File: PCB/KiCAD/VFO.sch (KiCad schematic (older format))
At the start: 23 parts, among them CON1 AVR-ISP-6, J1 USB_OTG, U10 LD1117S33TR, U2 ATMEGA8-16AU, U3 ADuM1201CR, U6 FT232RL, U7 SI5351, Y7 8Mhz, Y8 27Mhz

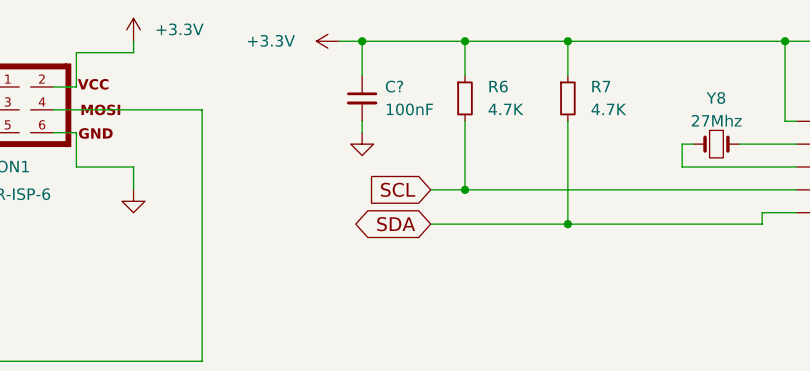
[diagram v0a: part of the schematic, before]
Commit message: diode mixer on discrete components, begin move to DragonFly libs
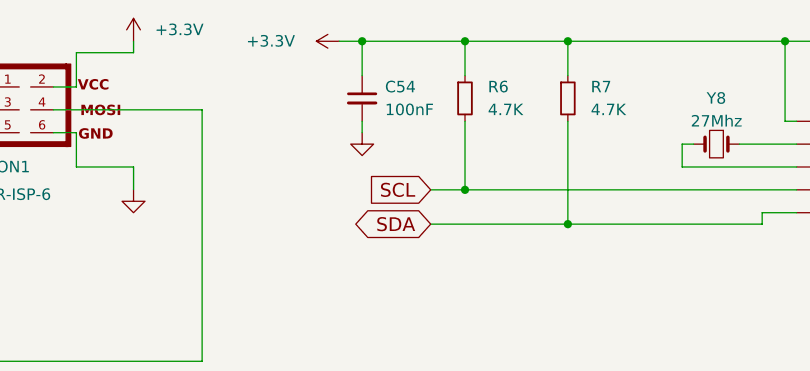
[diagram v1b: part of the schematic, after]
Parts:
- U10: footprint TO_SOT_Packages_SMD:SOT-223 -> DragonFly:SOT-223
- U3: footprint Housings_SOIC:SOIC-8_3.9x4.9mm_Pitch1.27mm -> DragonFly:SOIC-8_3.9x4.9mm_Pitch1.27mm
- gave numbers to parts that had none: 1
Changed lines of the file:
@@
 EESchema Schematic File Version 2
 LIBS:DragonFly-rescue
-LIBS:bee-rescue
 LIBS:power
 LIBS:device
@@
 $EndComp
 $Comp
-L GND #PWR39
+L GND #PWR023
 U 1 1 589EB3CB
 P 6100 1350
-F 0 "#PWR39" H 6100 1100 50  0001 C CNN
+F 0 "#PWR023" H 6100 1100 50  0001 C CNN
 F 1 "GND" H 6100 1200 50  0001 C CNN
 F 2 "" H 6100 1350 50  0000 C CNN
@@
 $EndComp
 $Comp
-L GND #PWR24
+L GND #PWR024
 U 1 1 589EFCBC
 P 750 2350
-F 0 "#PWR24" H 750 2100 50  0001 C CNN
+F 0 "#PWR024" H 750 2100 50  0001 C CNN
 F 1 "GND" H 750 2200 50  0001 C CNN
 F 2 "" H 750 2350 50  0000 C CNN
@@
 $EndComp
 $Comp
-L GND #PWR25
+L GND #PWR025
 U 1 1 589EFDB6
 P 750 2800
-F 0 "#PWR25" H 750 2550 50  0001 C CNN
+F 0 "#PWR025" H 750 2550 50  0001 C CNN
 F 1 "GND" H 750 2650 50  0001 C CNN
 F 2 "" H 750 2800 50  0000 C CNN
@@
 $EndComp
 $Comp
-L +3.3V #PWR41
+L +3.3V #PWR026
 U 1 1 58A03CC8
 P 7000 700
-F 0 "#PWR41" H 7000 550 50  0001 C CNN
+F 0 "#PWR026" H 7000 550 50  0001 C CNN
 F 1 "+3.3V" V 7000 1000 50  0000 C CNN
 F 2 "" H 7000 700 50  0000 C CNN
@@
 $EndComp
 $Comp
-L GND #PWR31
+L GND #PWR027
 U 1 1 58A061EE
 P 2850 6550
-F 0 "#PWR31" H 2850 6300 50  0001 C CNN
+F 0 "#PWR027" H 2850 6300 50  0001 C CNN
 F 1 "GND" H 2850 6400 50  0001 C CNN
 F 2 "" H 2850 6550 50  0000 C CNN
@@
 $EndComp
 $Comp
-L GND #PWR32
+L GND #PWR028
 U 1 1 58A09E30
 P 3400 6900
-F 0 "#PWR32" H 3400 6650 50  0001 C CNN
+F 0 "#PWR028" H 3400 6650 50  0001 C CNN
 F 1 "GND" H 3400 6750 50  0001 C CNN
 F 2 "" H 3400 6900 50  0000 C CNN
@@
 $EndComp
 $Comp
-L GND #PWR33
+L GND #PWR029
 U 1 1 58A0C9D9
 P 4150 6900
-F 0 "#PWR33" H 4150 6650 50  0001 C CNN
+F 0 "#PWR029" H 4150 6650 50  0001 C CNN
 F 1 "GND" H 4150 6750 50  0001 C CNN
 F 2 "" H 4150 6900 50  0000 C CNN
@@
 BFO_TX
 $Comp
-L GND #PWR48
+L GND #PWR030
 U 1 1 58E0B7EA
 P 10400 1250
-F 0 "#PWR48" H 10400 1000 50  0001 C CNN
+F 0 "#PWR030" H 10400 1000 50  0001 C CNN
 F 1 "GND" H 10400 1100 50  0001 C CNN
 F 2 "" H 10400 1250 50  0000 C CNN
@@
 SCL
 $Comp
-L +3.3V #PWR38
+L +3.3V #PWR031
 U 1 1 60FBBB98
 P 6100 700
-F 0 "#PWR38" H 6100 550 50  0001 C CNN
+F 0 "#PWR031" H 6100 550 50  0001 C CNN
 F 1 "+3.3V" H 6300 750 50  0000 C CNN
 F 2 "" H 6100 700 50  0000 C CNN
@@
 F 0 "U3" H 4750 4600 50  0000 L CNN
 F 1 "ADuM1201CR" H 5100 4600 50  0000 L CNN
-F 2 "Housings_SOIC:SOIC-8_3.9x4.9mm_Pitch1.27mm" H 5100 4200 50  0001 C CIN
+F 2 "DragonFly:SOIC-8_3.9x4.9mm_Pitch1.27mm" H 5100 4200 50  0001 C CIN
 F 3 "" H 5100 4200 50  0001 C CNN
 	1    5100 4200
@@
 $EndComp
 $Comp
-L GND #PWR35
+L GND #PWR032
 U 1 1 60FBEFE8
 P 4550 4450
-F 0 "#PWR35" H 4550 4200 50  0001 C CNN
+F 0 "#PWR032" H 4550 4200 50  0001 C CNN
 F 1 "GND" H 4550 4300 50  0001 C CNN
 F 2 "" H 4550 4450 50  0000 C CNN
@@
 $EndComp
 $Comp
-L +3.3V #PWR34
+L +3.3V #PWR033
 U 1 1 60FBF348
 P 4550 3950
-F 0 "#PWR34" H 4550 3800 50  0001 C CNN
+F 0 "#PWR033" H 4550 3800 50  0001 C CNN
 F 1 "+3.3V" V 4550 4200 50  0000 C CNN
 F 2 "" H 4550 3950 50  0000 C CNN
@@
 $EndComp
 $Comp
-L GNDD #PWR44
+L GNDD #PWR034
 U 1 1 60FC3E83
 P 8650 4700
-F 0 "#PWR44" H 8650 4450 50  0001 C CNN
+F 0 "#PWR034" H 8650 4450 50  0001 C CNN
 F 1 "GNDD" H 8650 4575 50  0001 C CNN
 F 2 "" H 8650 4700 50  0001 C CNN
@@
 $EndComp
 $Comp
-L GNDD #PWR43
+L GNDD #PWR035
 U 1 1 60FC3F82
 P 8650 4000
-F 0 "#PWR43" H 8650 3750 50  0001 C CNN
+F 0 "#PWR035" H 8650 3750 50  0001 C CNN
 F 1 "GNDD" H 8650 3875 50  0001 C CNN
 F 2 "" H 8650 4000 50  0001 C CNN
@@
 $EndComp
 $Comp
-L GNDD #PWR47
+L GNDD #PWR036
 U 1 1 60FC3FE1
 P 10250 4750
-F 0 "#PWR47" H 10250 4500 50  0001 C CNN
+F 0 "#PWR036" H 10250 4500 50  0001 C CNN
 F 1 "GNDD" H 10250 4625 50  0001 C CNN
 F 2 "" H 10250 4750 50  0001 C CNN
@@
 $EndComp
 $Comp
-L GNDD #PWR37
+L GNDD #PWR037
 U 1 1 60FC45C5
 P 5650 4450
-F 0 "#PWR37" H 5650 4200 50  0001 C CNN
+F 0 "#PWR037" H 5650 4200 50  0001 C CNN
 F 1 "GNDD" H 5650 4325 50  0001 C CNN
 F 2 "" H 5650 4450 50  0001 C CNN
@@
 $EndComp
 $Comp
-L GNDD #PWR40
+L GNDD #PWR038
 U 1 1 60FC465C
 P 7000 5900
-F 0 "#PWR40" H 7000 5650 50  0001 C CNN
+F 0 "#PWR038" H 7000 5650 50  0001 C CNN
 F 1 "GNDD" H 7000 5775 50  0001 C CNN
 F 2 "" H 7000 5900 50  0001 C CNN
@@
 $EndComp
 $Comp
-L GNDD #PWR45
+L GNDD #PWR039
 U 1 1 60FC82A8
 P 8700 3600
-F 0 "#PWR45" H 8700 3350 50  0001 C CNN
+F 0 "#PWR039" H 8700 3350 50  0001 C CNN
 F 1 "GNDD" H 8700 3475 50  0001 C CNN
 F 2 "" H 8700 3600 50  0001 C CNN
@@
 $EndComp
 $Comp
-L GNDD #PWR46
+L GNDD #PWR040
 U 1 1 60FC8353
 P 9650 3600
-F 0 "#PWR46" H 9650 3350 50  0001 C CNN
+F 0 "#PWR040" H 9650 3350 50  0001 C CNN
 F 1 "GNDD" H 9650 3475 50  0001 C CNN
 F 2 "" H 9650 3600 50  0001 C CNN
@@
 $EndComp
 $Comp
-L GNDD #PWR42
+L GNDD #PWR041
 U 1 1 60FC83BE
 P 7600 3550
-F 0 "#PWR42" H 7600 3300 50  0001 C CNN
+F 0 "#PWR041" H 7600 3300 50  0001 C CNN
 F 1 "GNDD" H 7600 3425 50  0001 C CNN
 F 2 "" H 7600 3550 50  0001 C CNN
@@
 $EndComp
 $Comp
-L +3.3V #PWR30
+L +3.3V #PWR042
 U 1 1 60FCB4EA
 P 2650 1250
-F 0 "#PWR30" H 2650 1100 50  0001 C CNN
+F 0 "#PWR042" H 2650 1100 50  0001 C CNN
 F 1 "+3.3V" H 2850 1300 50  0000 C CNN
 F 2 "" H 2650 1250 50  0000 C CNN
@@
 	4950 1450 1600 1450
 $Comp
-L GND #PWR29
+L GND #PWR043
 U 1 1 60FCC081
 P 2600 4550
-F 0 "#PWR29" H 2600 4300 50  0001 C CNN
+F 0 "#PWR043" H 2600 4300 50  0001 C CNN
 F 1 "GND" H 2600 4400 50  0001 C CNN
 F 2 "" H 2600 4550 50  0000 C CNN
@@
 Connection ~ 2600 4500
 $Comp
-L +3.3V #PWR36
+L +3.3V #PWR044
 U 1 1 60FCC6C5
 P 4700 6250
-F 0 "#PWR36" H 4700 6100 50  0001 C CNN
+F 0 "#PWR044" H 4700 6100 50  0001 C CNN
 F 1 "+3.3V" V 4700 6500 50  0000 C CNN
 F 2 "" H 4700 6250 50  0000 C CNN
@@
 $EndComp
 $Comp
-L +12V #PWR28
+L +12V #PWR045
 U 1 1 60FCCDC8
 P 2300 6150
-F 0 "#PWR28" H 2300 6000 50  0001 C CNN
+F 0 "#PWR045" H 2300 6000 50  0001 C CNN
 F 1 "+12V" H 2300 6290 50  0000 C CNN
 F 2 "" H 2300 6150 50  0000 C CNN
@@
 F 0 "U10" H 2850 6600 50  0000 C CNN
 F 1 "LD1117S33TR" H 2850 6500 50  0000 C CNN
-F 2 "TO_SOT_Packages_SMD:SOT-223" H 2850 6400 50  0001 C CNN
+F 2 "DragonFly:SOT-223" H 2850 6400 50  0001 C CNN
 F 3 "" H 2850 6300 50  0000 C CNN
 	1    2850 6300
@@
 TX_TRX
 $Comp
-L GND #PWR27
+L GND #PWR046
 U 1 1 60FE3270
 P 1650 2200
-F 0 "#PWR27" H 1650 1950 50  0001 C CNN
+F 0 "#PWR046" H 1650 1950 50  0001 C CNN
 F 1 "GND" H 1650 2050 50  0001 C CNN
 F 2 "" H 1650 2200 50  0000 C CNN
@@
 $EndComp
 $Comp
-L GND #PWR26
+L GND #PWR047
 U 1 1 610504BE
 P 1150 2100
-F 0 "#PWR26" H 1150 1850 50  0001 C CNN
+F 0 "#PWR047" H 1150 1850 50  0001 C CNN
 F 1 "GND" H 1150 1950 50  0001 C CNN
 F 2 "" H 1150 2100 50  0000 C CNN
@@
 	4400 2600 3650 2600
 $Comp
-L C_Small C?
+L C_Small C54
 U 1 1 61063DA5
 P 7100 950
-F 0 "C?" H 7200 1000 50  0000 L CNN
+F 0 "C54" H 7200 1000 50  0000 L CNN
 F 1 "100nF" H 7200 900 50  0000 L CNN
 F 2 "Capacitors_SMD:C_0603_HandSoldering" H 7100 950 50  0001 C CNN
@@
 $EndComp
 $Comp
-L GND #PWR?
+L GND #PWR048
 U 1 1 61063FC6
 P 7100 1100
-F 0 "#PWR?" H 7100 850 50  0001 C CNN
+F 0 "#PWR048" H 7100 850 50  0001 C CNN
 F 1 "GND" H 7100 950 50  0001 C CNN
 F 2 "" H 7100 1100 50  0000 C CNN
